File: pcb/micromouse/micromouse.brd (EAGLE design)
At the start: 81.5 x 99.2 mm, 55 parts, among them J1 Connector_M1, J2 Connector_M2, J4 Programmer

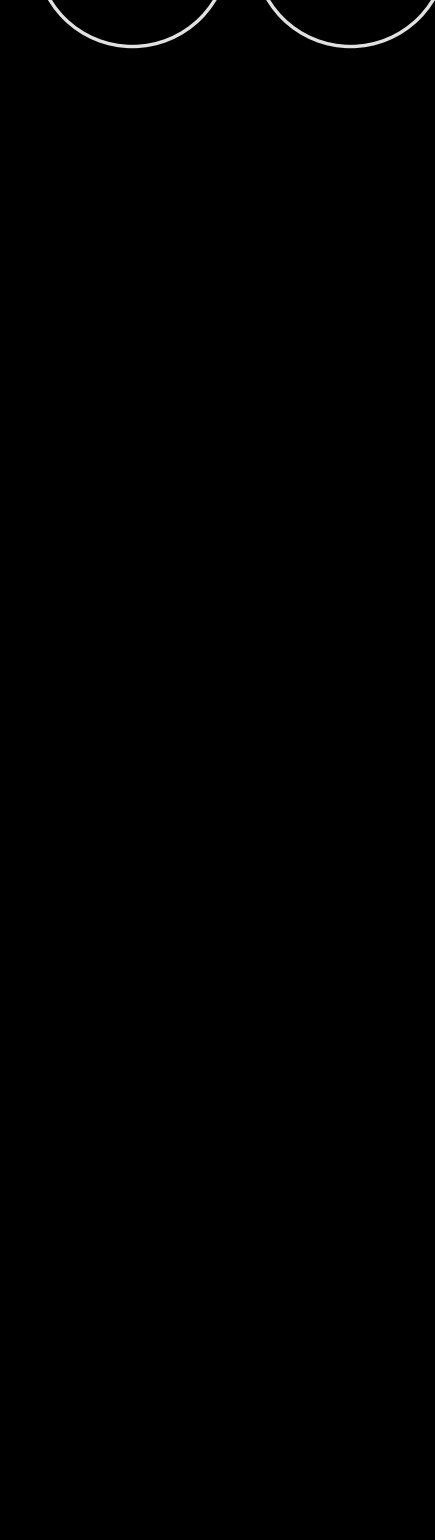
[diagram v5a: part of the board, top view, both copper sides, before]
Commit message: Add test points
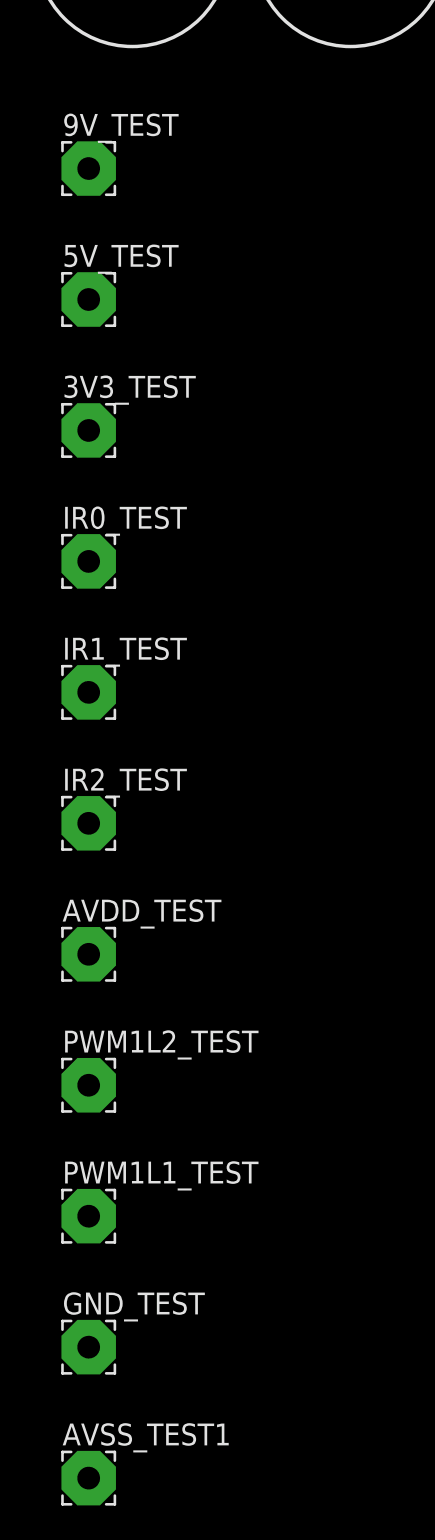
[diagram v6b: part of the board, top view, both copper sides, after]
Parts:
- added 3V3_TEST, 5V_TEST, 9V_TEST, AVDD_TEST, AVSS_TEST1, GND_TEST, IR0_TEST, IR1_TEST, IR2_TEST, PWM1L1_TEST, PWM1L2_TEST: (no value), wirepad:3,17/1,3
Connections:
- net +3V3: now also 3V3_TEST.1
- net +5V: now also 5V_TEST.1
- net +9V: now also 9V_TEST.1
- net AVDD: now also AVDD_TEST.1
- net AVSS: now also AVSS_TEST1.1
- net GND: now also GND_TEST.1
- net IR0: now also IR0_TEST.1
- net IR1: now also IR1_TEST.1
- net IR2: now also IR2_TEST.1
- net PWM1L1: now also PWM1L1_TEST.1
- net PWM1L2: now also PWM1L2_TEST.1

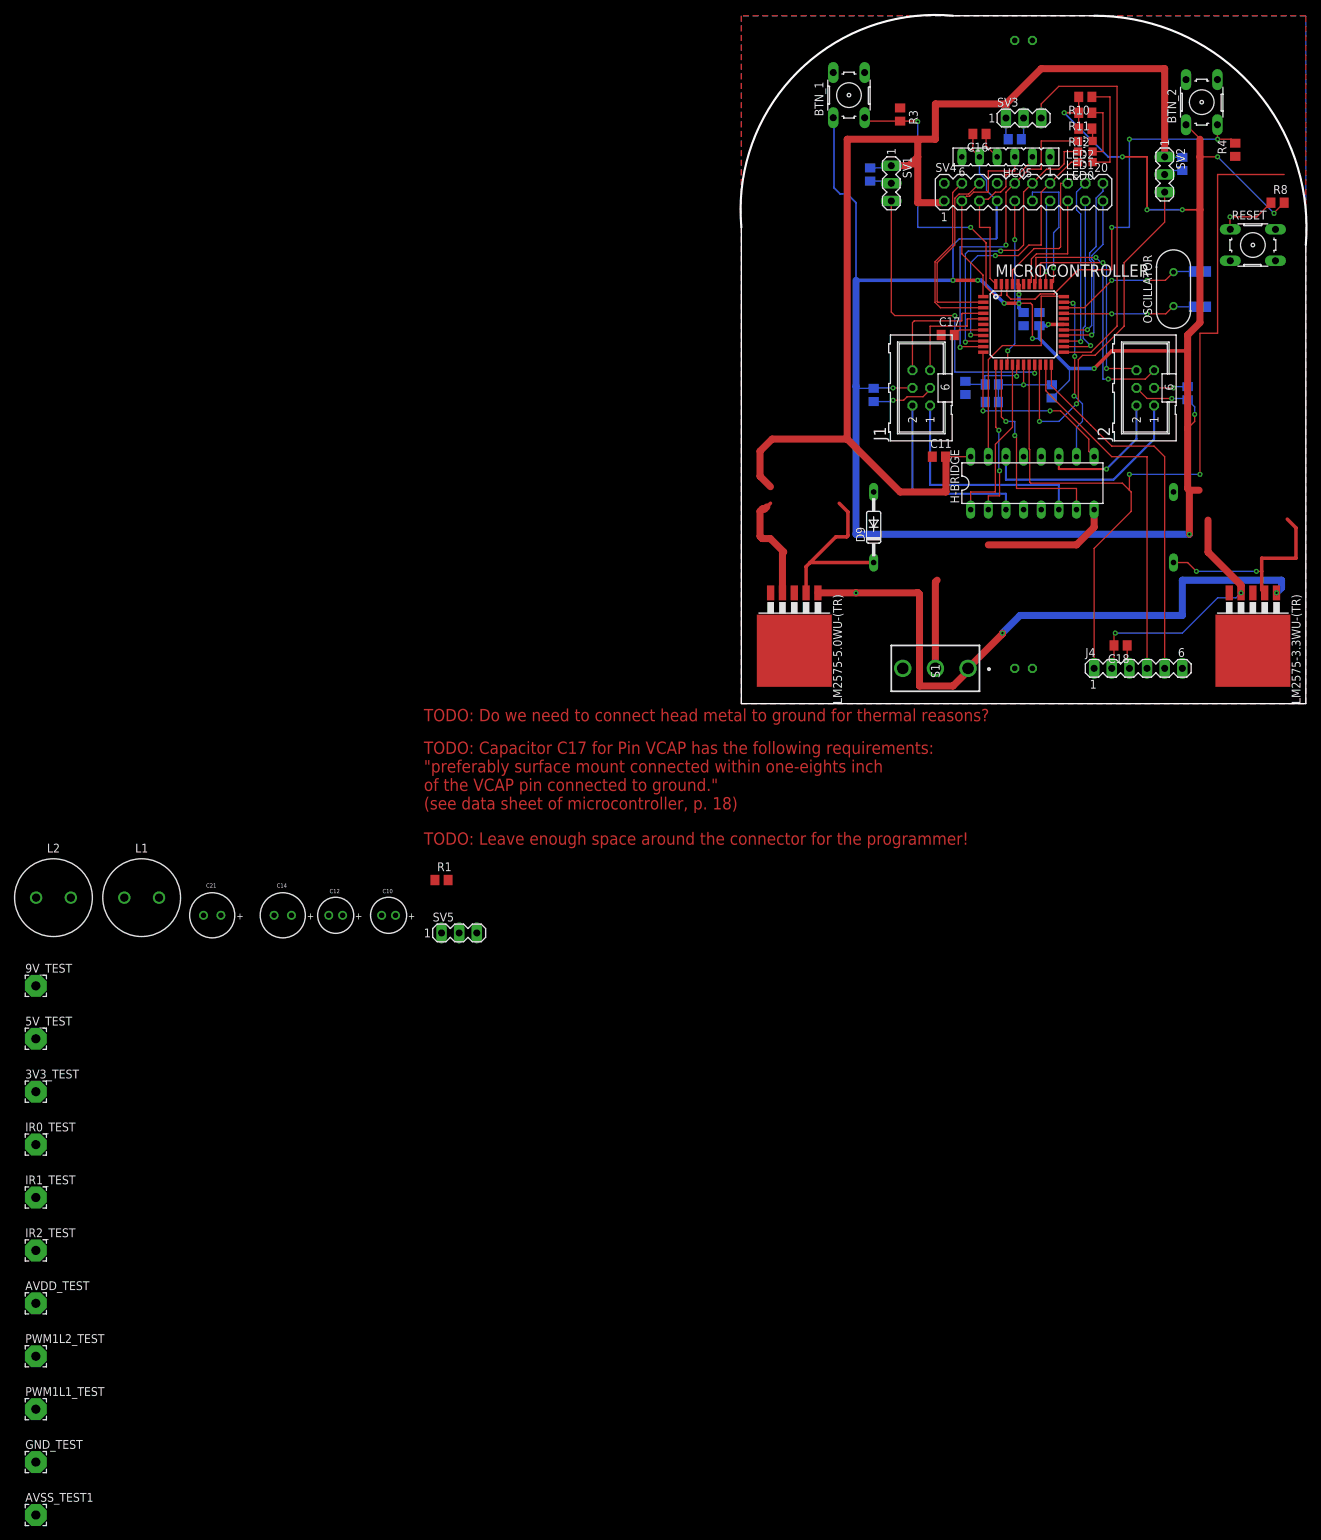
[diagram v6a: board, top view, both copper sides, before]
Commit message: Increase width of lanes, all 45 degree angles errors resolved design rules obeyed
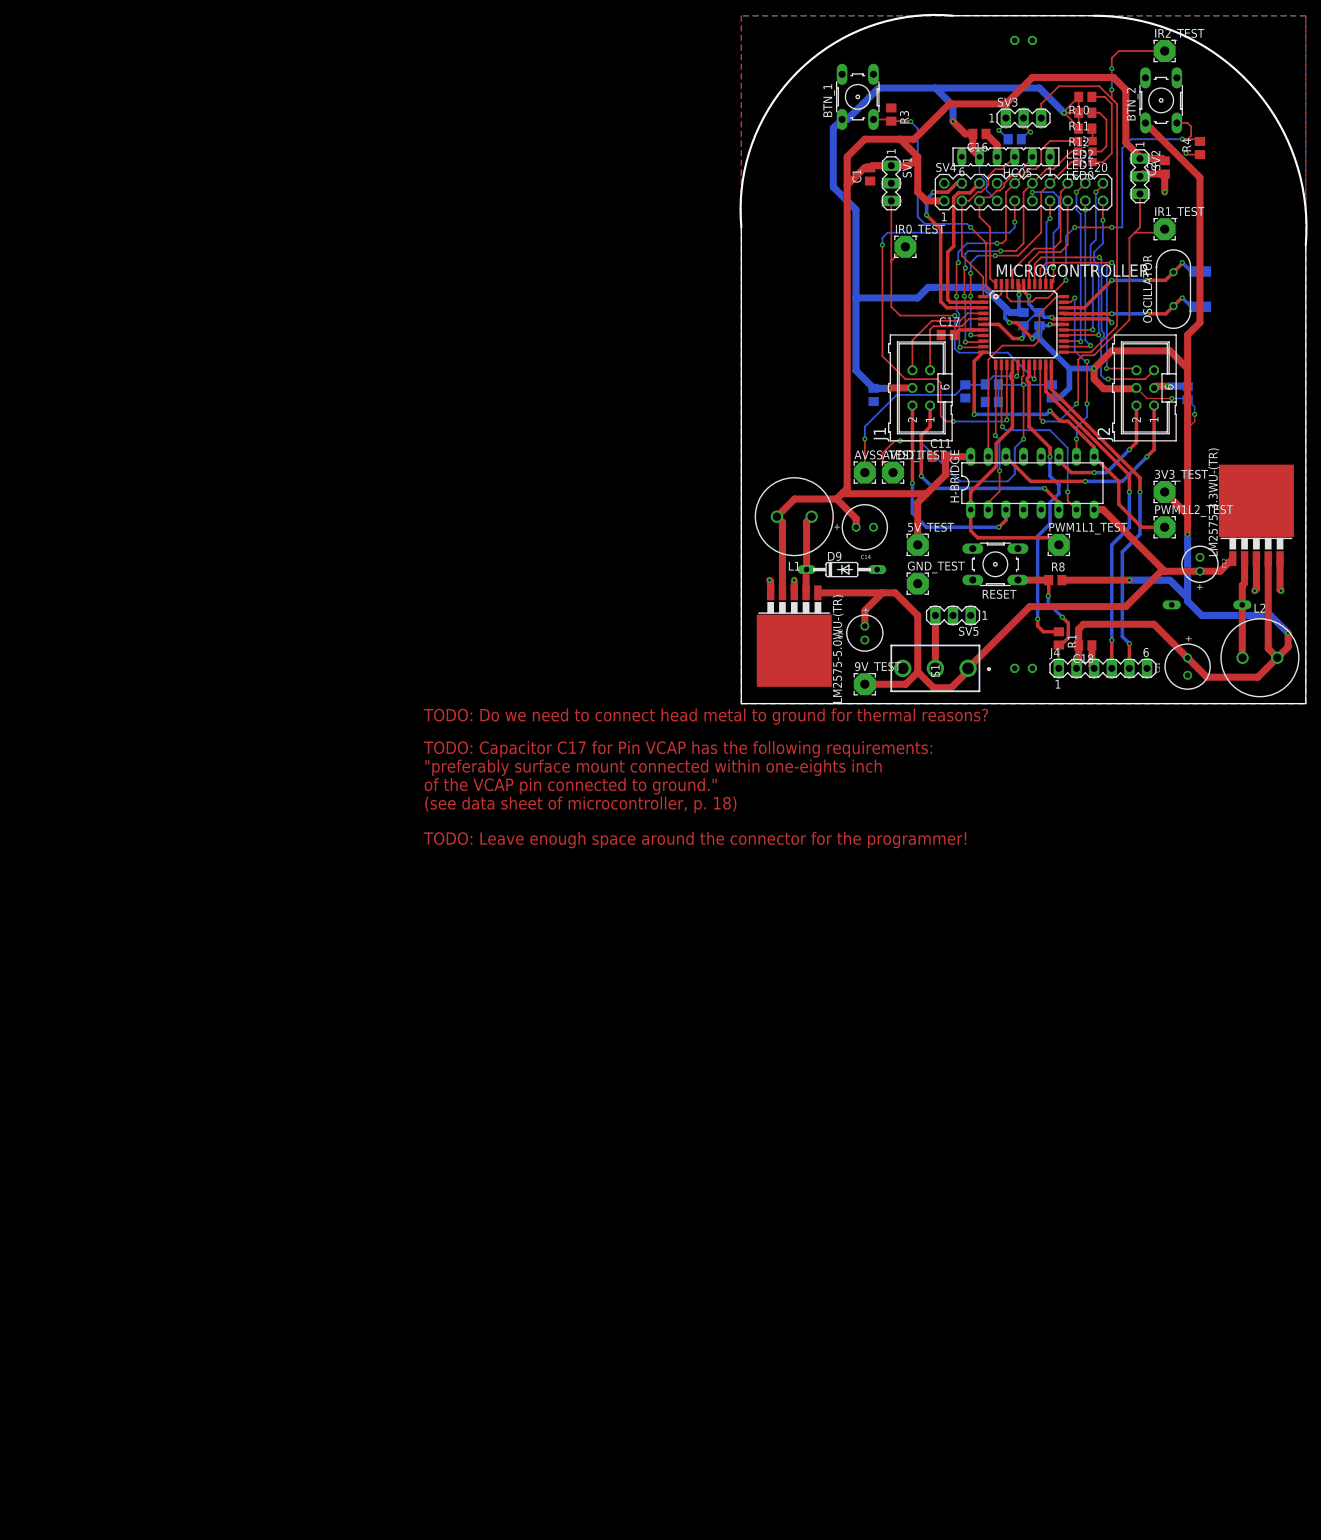
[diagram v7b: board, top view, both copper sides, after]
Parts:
- moved IR2_TEST 237.2 mm to (61.0, 94.0)
- moved IR1_TEST 214.2 mm to (61.0, 68.3)
- moved PWM1L2_TEST 201.7 mm to (61.0, 25.4)
- moved PWM1L1_TEST 192.9 mm to (45.7, 22.9)
- moved AVSS_TEST1 191.8 mm to (17.8, 33.3)
- moved 3V3_TEST 184.1 mm to (61.0, 30.5)
- moved IR0_TEST 180.0 mm to (23.6, 65.8)
- moved GND_TEST 179.2 mm to (25.4, 17.3)
- moved L2 177.1 mm to (74.7, 6.60)
- moved AVDD_TEST 171.9 mm to (21.8, 33.3)
- moved 5V_TEST 145.6 mm to (25.4, 22.9)
- moved C21 145.0 mm to (64.3, 5.33), turned to 90 degrees
- moved C12 134.3 mm to (66.0, 20.1), turned to 270 degrees
- moved 9V_TEST 127.0 mm to (17.8, 2.79)
- moved L1 108.8 mm to (7.62, 26.9), turned to 180 degrees
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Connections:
- new net N$1: MICROCONTROLLER.18, R1.1
- net N_MCLR: no longer MICROCONTROLLER.18, R1.1
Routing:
- net N_MCLR: track 136.2 -> 19.1 mm, vias 3 -> 2
- net IO0: track 24.0 -> 73.2 mm, vias 2 -> 4
- net N$1: track 0.00 -> 48.6 mm, vias 0 -> 2
- net AVDD: track 13.2 -> 52.8 mm, vias 1 -> 3
- net GND: track 31.1 -> 65.4 mm, vias 2 -> 12
- net AVSS: track 10.7 -> 33.2 mm, vias 1 -> 2
- net PWM1L2: track 28.2 -> 46.8 mm
- net N$8: track 29.5 -> 14.4 mm, vias 2 -> 0
- net N$7: track 26.0 -> 11.3 mm
- net PWM1L1: track 25.4 -> 40.1 mm
- net +3V3: track 397.9 -> 384.8 mm, vias 20 -> 13
- net IR2: track 57.8 -> 70.2 mm, vias 0 -> 2
- net +5V: track 208.6 -> 197.3 mm, vias 0 -> 1
- net N$2: track 12.8 -> 7.62 mm
- net +9V: track 111.0 -> 106.1 mm, vias 3 -> 0
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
